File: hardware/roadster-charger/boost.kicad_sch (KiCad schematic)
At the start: 26 parts, among them Q1 NMOS, Q2 NMOS, U4 LTC3786EUD#TRPBF, U5 DAC70501MDQFR

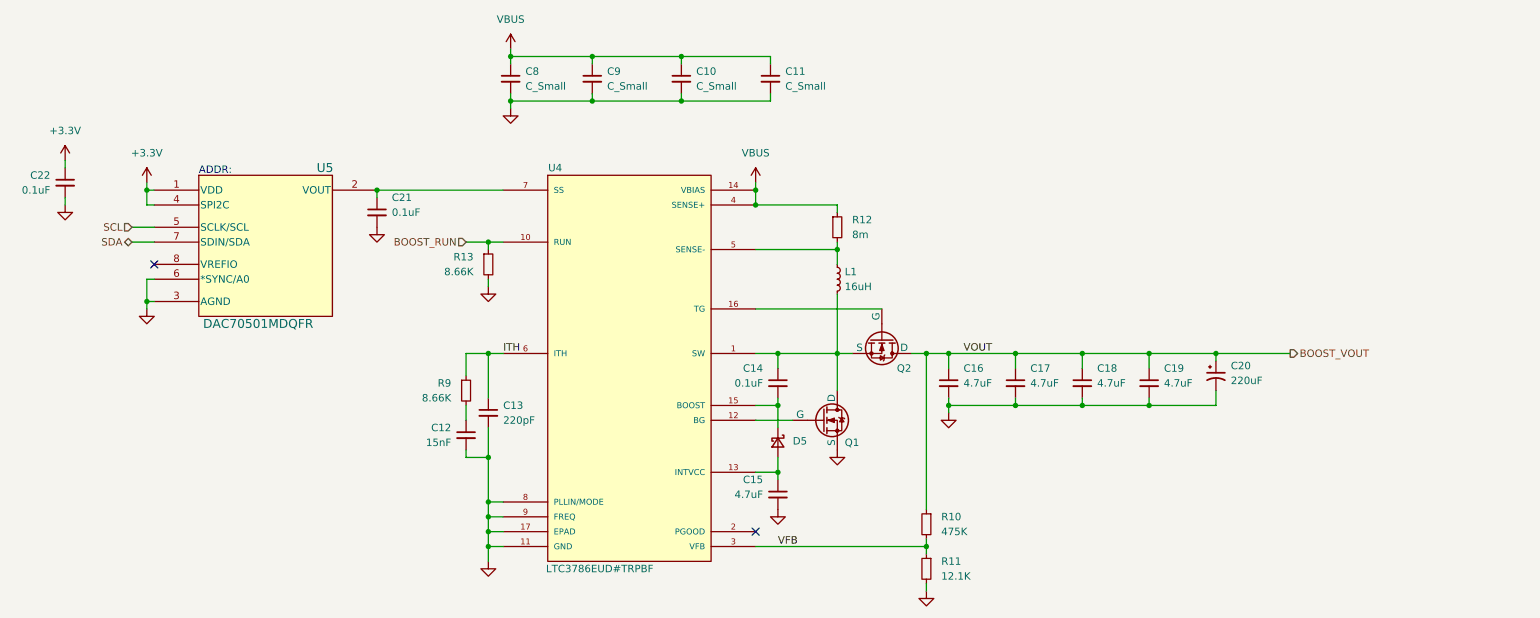
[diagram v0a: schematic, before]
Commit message: add buffer to I_SENSE
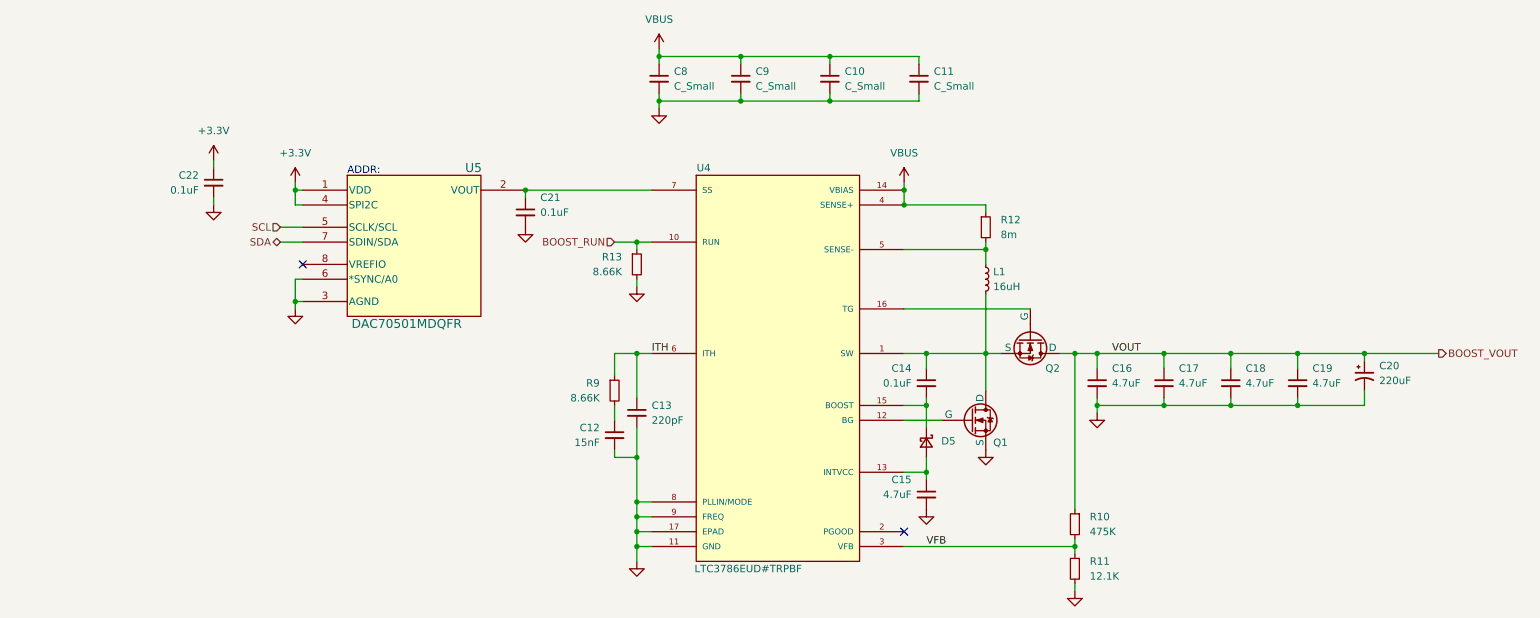
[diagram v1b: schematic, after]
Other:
- moved on the sheet: C10, C11, C12, C13, C14, C15, C16, C17, C18, C19, C20, C21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

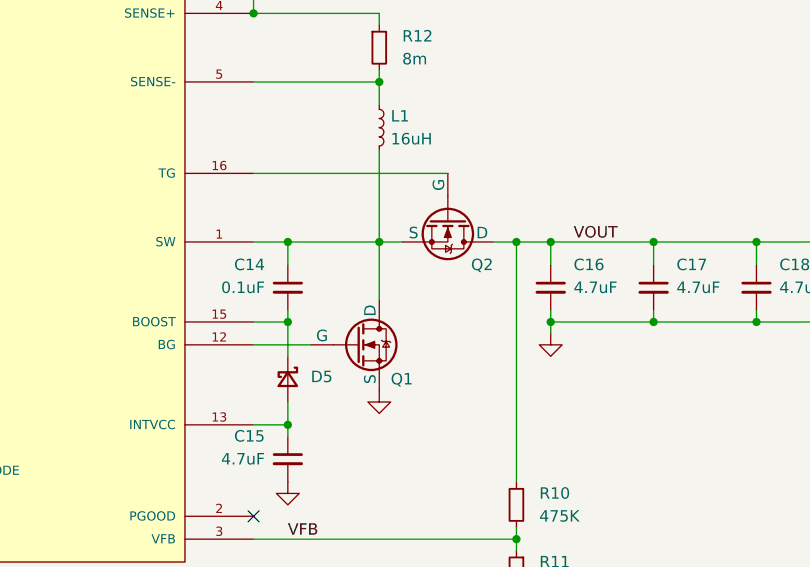
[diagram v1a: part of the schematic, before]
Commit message: add readme, swap out lv buck, swap n fets
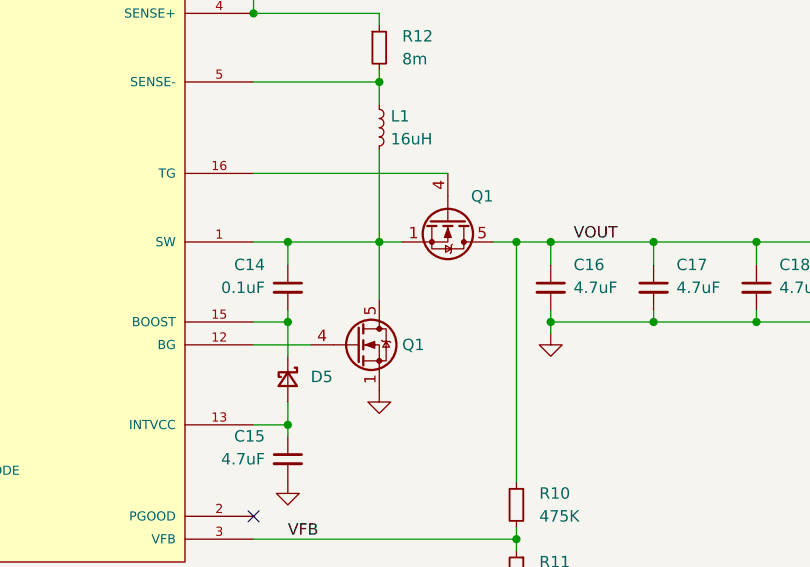
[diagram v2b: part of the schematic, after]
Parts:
- removed Q1, Q2: NMOS, symbol Simulation_SPICE:NMOS
- added Q1 (x2): CSD19532Q5B, Package_TO_SOT_SMD:TDSON-8-1, symbol Transistor_FET:CSD19532Q5B
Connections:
- net BOOST_VOUT: now also Q1.5 (D)
- net GND: now also Q1.1 (S), Q1.2 (S), Q1.3 (S)
- net at C14.1, L1.2, U4.1 (SW): now also Q1.1 (S), Q1.2 (S), Q1.3 (S), Q1.5 (D)
- net at U4.12 (BG): now also Q1.4 (G)
- net at U4.16 (TG): now also Q1.4 (G)
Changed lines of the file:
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@@
-    )
-  )
-  (symbol (lib_id "Simulation_SPICE:NMOS") (at 248.92 147.32 0) (unit 1)
-    (in_bom yes) (on_board yes) (dnp no)
-    (property "Reference" "Q1" (at 252.73 151.13 0)
-      (effects (font (size 1.27 1.27)) (justify left))
-    )
-    (property "Value" "NMOS" (at 255.27 148.59 0)
-      (effects (font (size 1.27 1.27)) (justify left) hide)
-    )
-    (property "Footprint" "" (at 254 144.78 0)
-      (effects (font (size 1.27 1.27)) hide)
-    )
-    (property "Datasheet" "https://ngspice.sourceforge.io/docs/ngspice-manual.pdf" (at 248.92 160.02 0)
-      (effects (font (size 1.27 1.27)) hide)
-    )
-    (property "Sim.Device" "NMOS" (at 248.92 164.465 0)
-      (effects (font (size 1.27 1.27)) hide)
-    )
-    (property "Sim.Type" "VDMOS" (at 248.92 166.37 0)
-      (effects (font (size 1.27 1.27)) hide)
-    )
-    (property "Sim.Pins" "1=D 2=G 3=S" (at 248.92 162.56 0)
-      (effects (font (size 1.27 1.27)) hide)
-    )
-    (pin "1")
-    (pin "2")
-    (pin "3")
-    (instances
-      (project "roadster-charger"
-        (path "/57ecac41-cd8a-4182-a81e-fed3e381aedd"
-          (reference "Q1") (unit 1)
-        )
-        (path "/57ecac41-cd8a-4182-a81e-fed3e381aedd/64ca4e4e-11ba-4e5c-8f8e-2432a1d47dd0"
-          (reference "Q3") (unit 1)
-        )
-      )
     )
   )
@@
     )
   )
+  (symbol (lib_id "Transistor_FET:CSD19532Q5B") (at 259.08 133.35 270) (unit 1)
+    (in_bom yes) (on_board yes) (dnp no)
+    (property "Reference" "Q1" (at 262.89 130.81 90)
+      (effects (font (size 1.27 1.27)))
+    )
+    (property "Value" "CSD19532Q5B" (at 259.08 142.24 90)
+      (effects (font (size 1.27 1.27)) hide)
+    )
+    (property "Footprint" "Package_TO_SOT_SMD:TDSON-8-1" (at 257.175 138.43 0)
+      (effects (font (size 1.27 1.27) italic) (justify left) hide)
+    )
+    (property "Datasheet" "http://www.ti.com/lit/gpn/csd19532q5b" (at 259.08 133.35 90)
+      (effects (font (size 1.27 1.27)) (justify left) hide)
+    )
+    (pin "1")
+    (pin "2")
+    (pin "3")
+    (pin "4")
+    (pin "5")
+    (instances
+      (project "roadster-charger"
+        (path "/57ecac41-cd8a-4182-a81e-fed3e381aedd"
+          (reference "Q1") (unit 1)
+        )
+        (path "/57ecac41-cd8a-4182-a81e-fed3e381aedd/64ca4e4e-11ba-4e5c-8f8e-2432a1d47dd0"
+          (reference "Q2") (unit 1)
+        )
+      )
+    )
+  )
   (symbol (lib_id "power:GND") (at 172.72 114.3 0) (unit 1)
     (in_bom yes) (on_board yes) (dnp no)
@@
         (path "/57ecac41-cd8a-4182-a81e-fed3e381aedd/64ca4e4e-11ba-4e5c-8f8e-2432a1d47dd0"
           (reference "D6") (unit 1)
+        )
+      )
+    )
+  )
+  (symbol (lib_id "Transistor_FET:CSD19532Q5B") (at 248.92 147.32 0) (unit 1)
+    (in_bom yes) (on_board yes) (dnp no)
+    (property "Reference" "Q1" (at 254 147.32 0)
+      (effects (font (size 1.27 1.27)) (justify left))
+    )
+    (property "Value" "CSD19532Q5B" (at 255.27 148.59 0)
+      (effects (font (size 1.27 1.27)) (justify left) hide)
+    )
+    (property "Footprint" "Package_TO_SOT_SMD:TDSON-8-1" (at 254 149.225 0)
+      (effects (font (size 1.27 1.27) italic) (justify left) hide)
+    )
+    (property "Datasheet" "http://www.ti.com/lit/gpn/csd19532q5b" (at 248.92 147.32 90)
+      (effects (font (size 1.27 1.27)) (justify left) hide)
+    )
+    (pin "1")
+    (pin "2")
+    (pin "3")
+    (pin "4")
+    (pin "5")
+    (instances
+      (project "roadster-charger"
+        (path "/57ecac41-cd8a-4182-a81e-fed3e381aedd"
+          (reference "Q1") (unit 1)
+        )
+        (path "/57ecac41-cd8a-4182-a81e-fed3e381aedd/64ca4e4e-11ba-4e5c-8f8e-2432a1d47dd0"
+          (reference "Q3") (unit 1)
         )
       )
@@
         )
       )
-    )
-  )
-  (symbol (lib_id "Simulation_SPICE:NMOS") (at 259.08 133.35 270) (unit 1)
-    (in_bom yes) (on_board yes) (dnp no)
-    (property "Reference" "Q2" (at 262.89 138.43 90)
-      (effects (font (size 1.27 1.27)))
-    )
-    (property "Value" "NMOS" (at 259.08 142.24 90)
-      (effects (font (size 1.27 1.27)) hide)
-    )
-    (property "Footprint" "" (at 261.62 138.43 0)
-      (effects (font (size 1.27 1.27)) hide)
-    )
-    (property "Datasheet" "https://ngspice.sourceforge.io/docs/ngspice-manual.pdf" (at 246.38 133.35 0)
-      (effects (font (size 1.27 1.27)) hide)
-    )
-    (property "Sim.Device" "NMOS" (at 241.935 133.35 0)
-      (effects (font (size 1.27 1.27)) hide)
-    )
-    (property "Sim.Type" "VDMOS" (at 240.03 133.35 0)
-      (effects (font (size 1.27 1.27)) hide)
-    )
-    (property "Sim.Pins" "1=D 2=G 3=S" (at 243.84 133.35 0)
-      (effects (font (size 1.27 1.27)) hide)
-    )
-    (pin "1")
-    (pin "2")
-    (pin "3")
-    (instances
-      (project "roadster-charger"
-        (path "/57ecac41-cd8a-4182-a81e-fed3e381aedd"
-          (reference "Q2") (unit 1)
-        )
-        (path "/57ecac41-cd8a-4182-a81e-fed3e381aedd/64ca4e4e-11ba-4e5c-8f8e-2432a1d47dd0"
-          (reference "Q4") (unit 1)
-        )
-      )

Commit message: schematic cleanup and labeling
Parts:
- removed C10, C11, C8, C9: C_Small, symbol Device:C_Small
- removed C17, C18, C19: 4.7uF, symbol Device:C_Small
- removed C20: 220uF, symbol Device:C_Polarized_Small_US
- added C16 (x7): 6.8uF, Capacitor_SMD:C_1812_4532Metric, symbol Device:C_Small
- C16: value 4.7uF -> 6.8uF; footprint (none) -> Capacitor_SMD:C_1812_4532Metric; MPN (none) -> C4532X7R1H685K
- L1: MPN (none) -> PA2050.163NL
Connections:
- net BOOST_VOUT: now also C16.1, C16.1, C16.1
- net GND: now also C16.2, C16.2, C16.2, C16.2, C16.2, C16.2, C16.2
- net VBUS: now also C16.1, C16.1, C16.1, C16.1

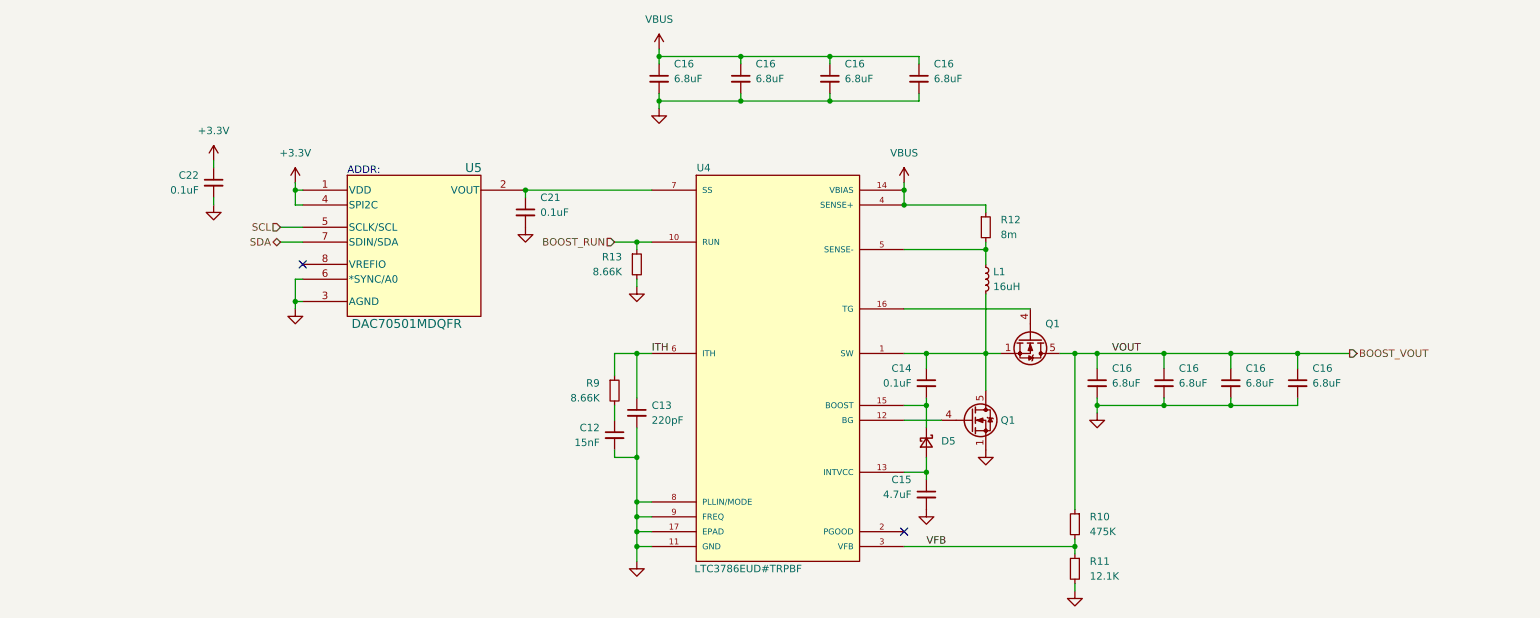
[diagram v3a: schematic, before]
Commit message: cleanup input current sense, assign some footprints
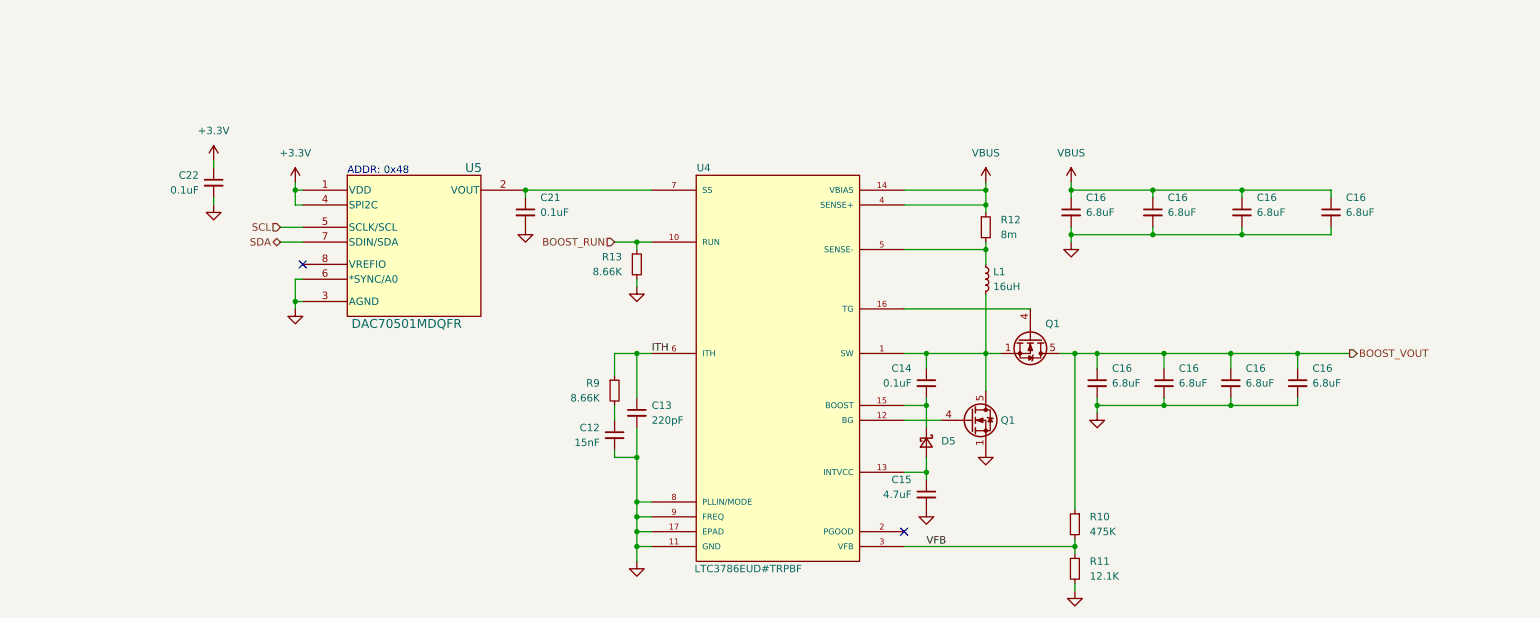
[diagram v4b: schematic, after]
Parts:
- D5: footprint (none) -> Diode_SMD:D_SOD-323
- L1: footprint (none) -> PA2050.193NL:IND_PA2050.193NL
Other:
- note added: "ADDR: 0x48"
- note removed: "ADDR:"
- moved on the sheet: C16
